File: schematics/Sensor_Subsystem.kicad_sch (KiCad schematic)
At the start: 0 parts

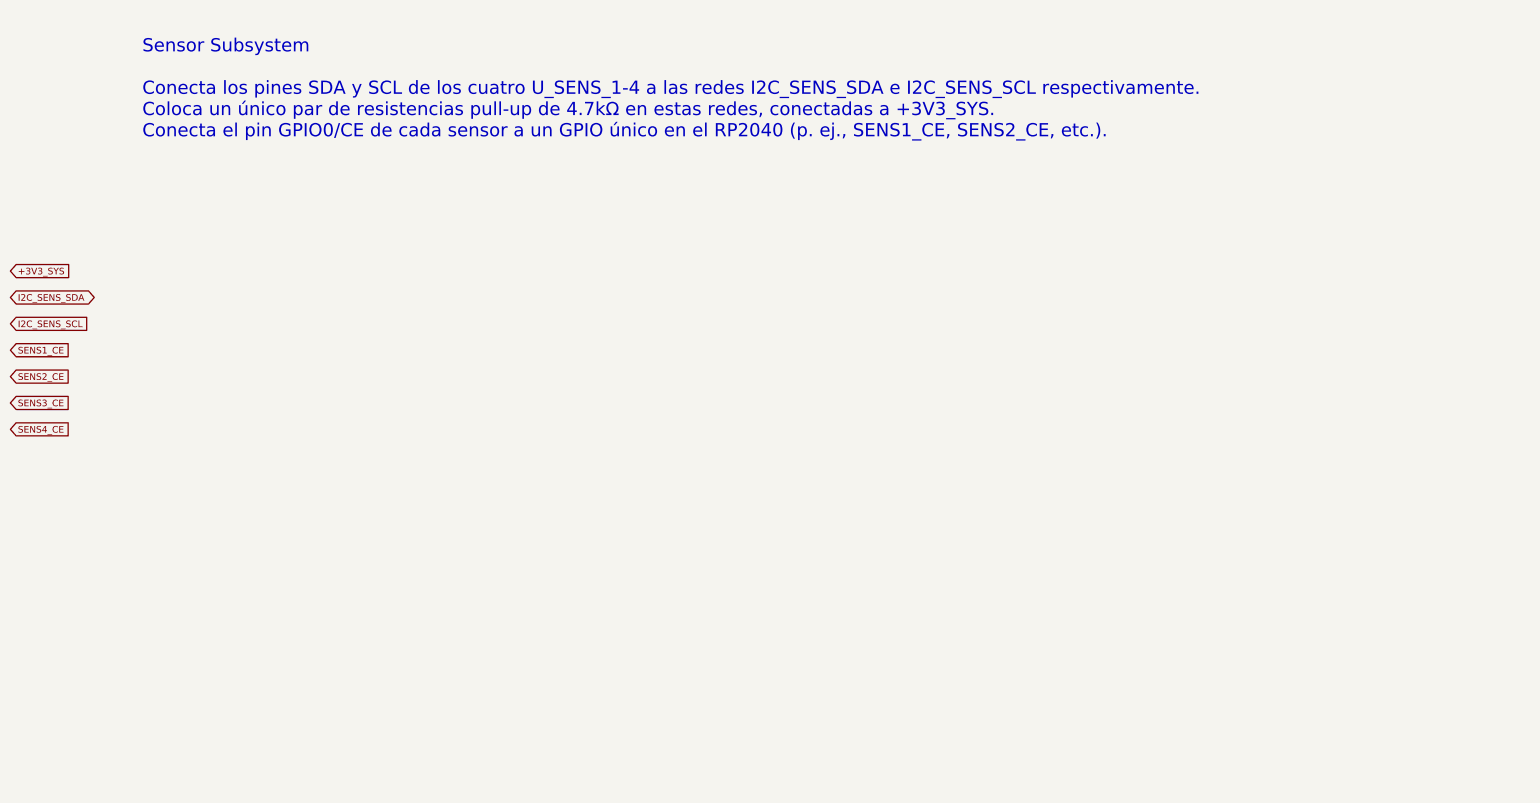
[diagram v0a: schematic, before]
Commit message: Añadir esquemático detallado del subsistema de sensores
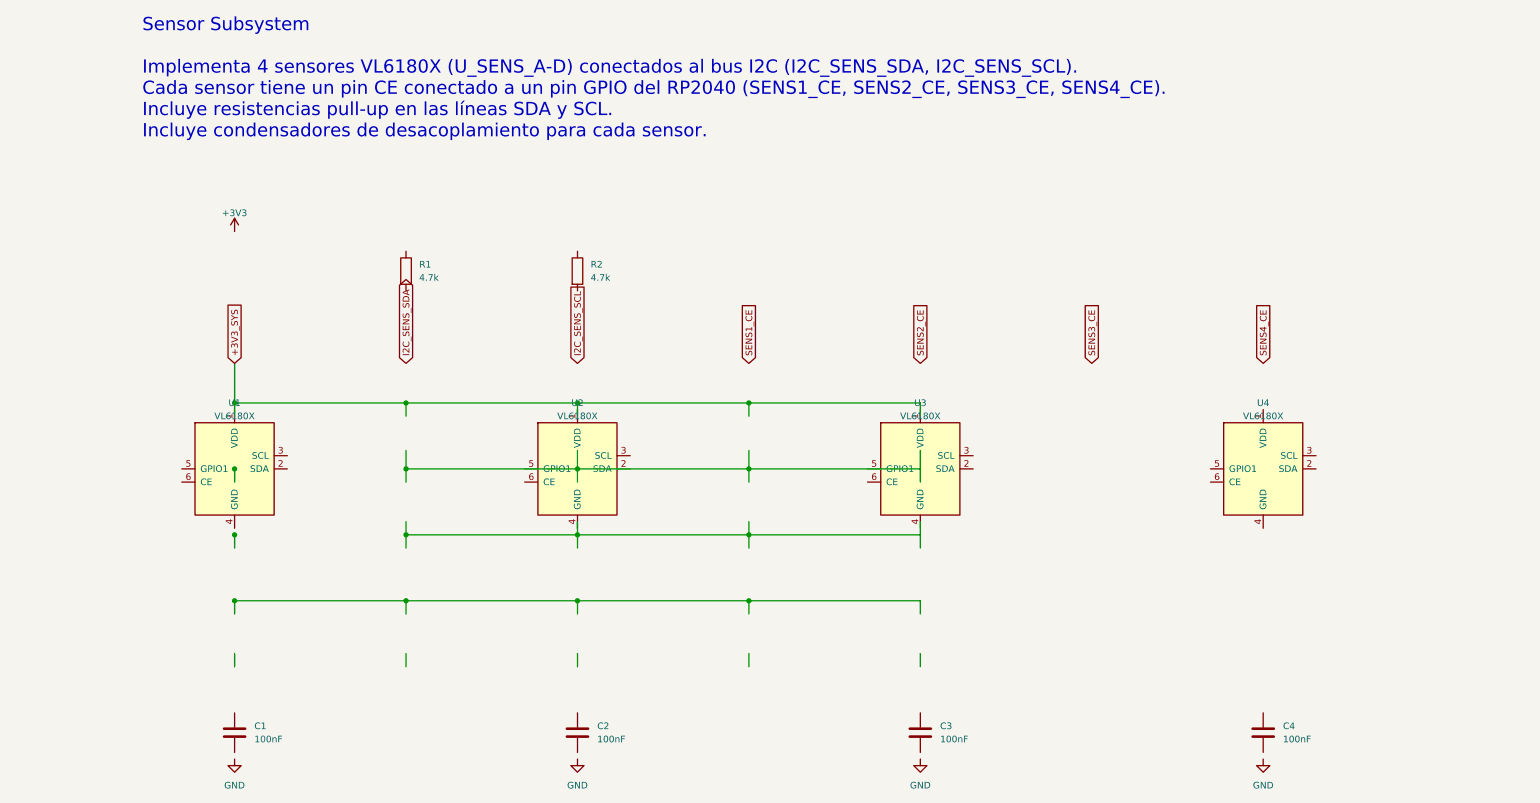
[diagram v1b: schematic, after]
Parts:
- added C1, C2, C3, C4: 100nF, Capacitor_SMD:C_0402_1005Metric, symbol Device:C
- added R1, R2: 4.7k, Resistor_SMD:R_0402_1005Metric, symbol Device:R
- added U1, U2, U3, U4: VL6180X, Package_LGA:LGA-12_2x2mm_P0.5mm, symbol custom_symbols:VL6180X
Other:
- note added: "Sensor Subsystem Implementa 4 sensores VL6180X (U_SENS_A-D) conectados al bus I2C (I2C_SENS_SDA, I2C_SENS_SCL). Cada sensor tiene un pin CE conectado a un pin GPIO del RP2040 (SENS1_CE, SENS2_CE, SENS3_CE, SENS4_CE). Incluye resistencias pull-up en las líneas SDA y SCL. Incluye condensadores de desacoplamiento para cada sensor."
- note removed: "Sensor Subsystem Conecta los pines SDA y SCL de los cuatro U_SENS_1-4 a las redes I2C_SENS_SDA e I2C_SENS_SCL respectivamente. Coloca un único par de resistencias pull-up de 4.7kΩ en estas redes, conectadas a +3V3_SYS. Conecta el pin GPIO0/CE de cada sensor a un GPIO único en el RP2040 (p. ej., SENS1_CE, SENS2_CE, etc.)."
